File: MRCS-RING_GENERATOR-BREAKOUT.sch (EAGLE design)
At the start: 9 parts

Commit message: Various updates while preparing documentation
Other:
- note added: "F connections for PCR SIN01 FO F1 0 0 25 Hz 0 1 17 Hz 1 = JMP to 5VREF"
- note removed: "F connections for PCR SIN06 FO F1 0 0 20Hz 0 1 25 Hz 1 0 17 Hz 1 1 50 Hz 0 = OPEN 1 = JMP to 5VREF doesn't seem to work for SIN01, F0-F1 sit near ground and pulling up to 5 or 12 doesn't change freq or Vout"
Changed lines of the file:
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@@
 <text x="241.3" y="6.35" size="2.1844" layer="97">A</text>
 <text x="166.37" y="6.35" size="2.1844" layer="97">Seth Neumann</text>
-<text x="5.08" y="7.62" size="1.778" layer="97">F connections for PCR SIN06
+<text x="5.08" y="7.62" size="1.778" layer="97">F connections for PCR SIN01
 FO F1
-0  0  20Hz
-0  1  25 Hz
-1  0  17 Hz
-1  1   50 Hz
-0 = OPEN
-1 = JMP to 5VREF
-doesn't seem to work for SIN01, F0-F1 sit near ground
-and pulling up to 5 or 12 doesn't change freq or Vout</text>
+0  0  25 Hz
+0  1  17 Hz
+1 = JMP to 5VREF</text>
 <text x="129.54" y="157.48" size="1.778" layer="91">F1     F0</text>
 <text x="91.44" y="124.46" size="1.778" layer="91">pads for 0.1",

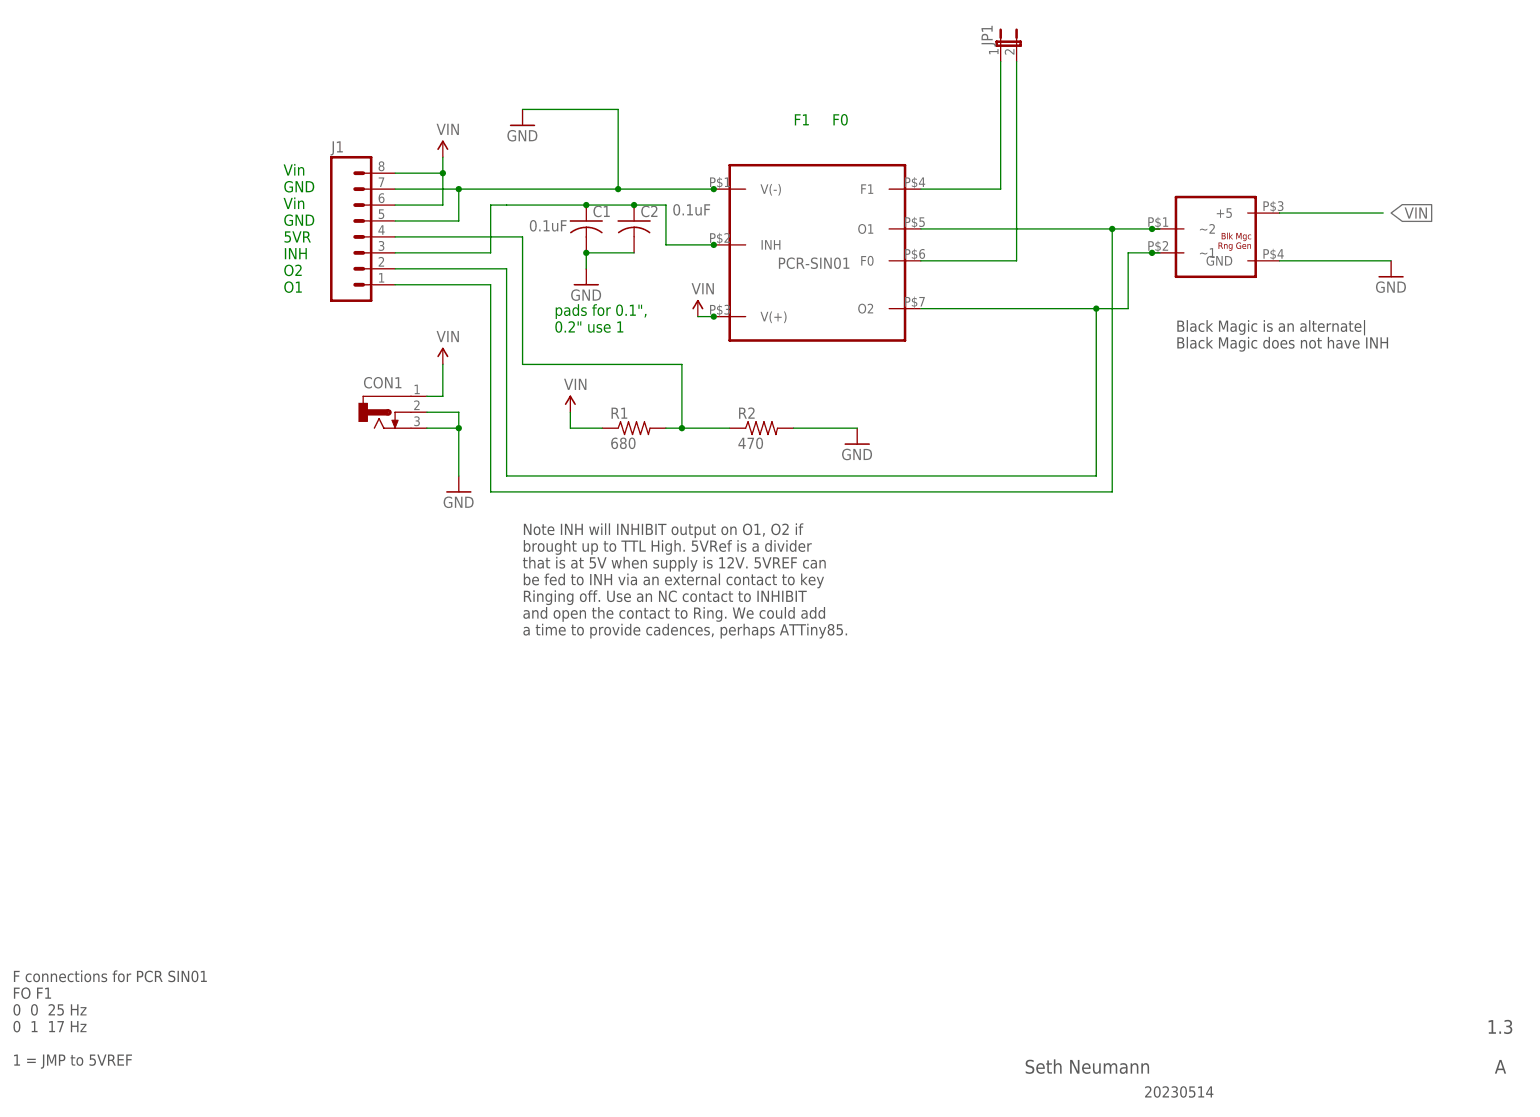
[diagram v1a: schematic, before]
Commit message: panelized 2 up version
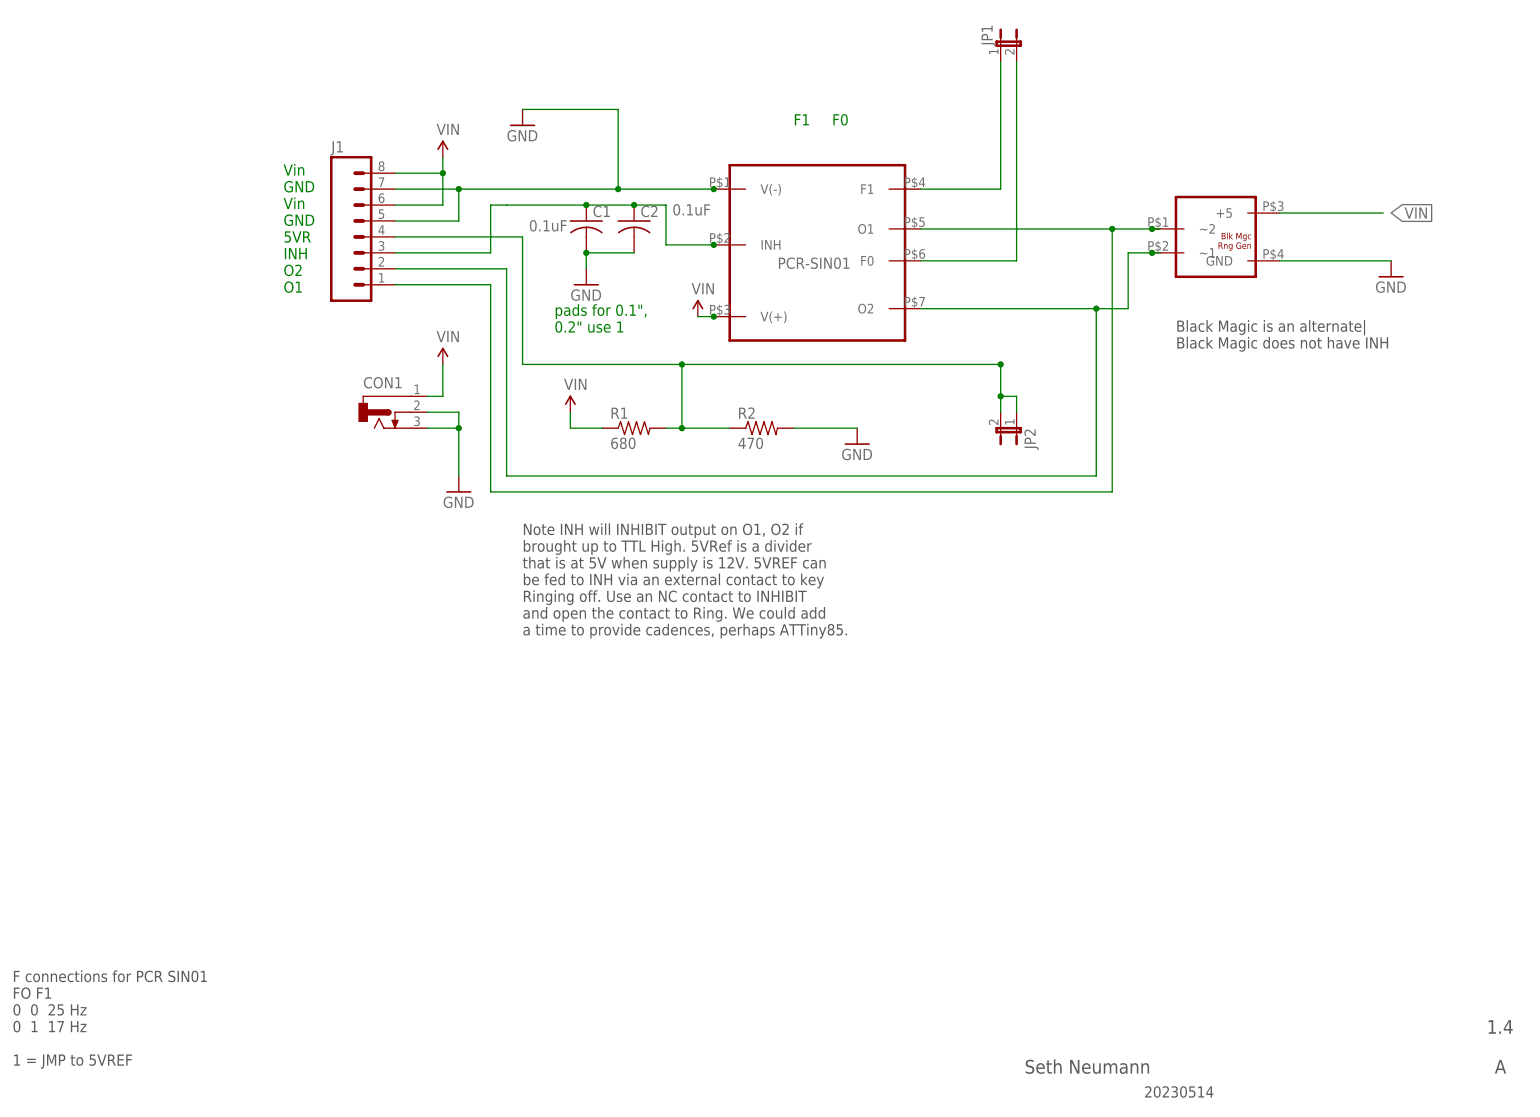
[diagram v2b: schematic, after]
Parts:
- added JP2: (no value), SPCoast:JUMPER-2PTH_LOCK
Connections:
- net 5VREF: now also JP2.1, JP2.2
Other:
- note added: "1.4"
- note removed: "1.3"
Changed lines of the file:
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@@
 <part name="U$5" library="MRCS" deviceset="BLACK_MAGIC_RING_GEN" device=""/>
 <part name="GND3" library="SPCoast" deviceset="GND" device=""/>
+<part name="JP2" library="SPCoast" deviceset="JUMPER-2" device="PTH_LOCK"/>
 </parts>
 <sheets>
 <sheet>
 <plain>
-<text x="240.03" y="12.7" size="2.1844" layer="97">1.3</text>
+<text x="240.03" y="12.7" size="2.1844" layer="97">1.4</text>
 <text x="241.3" y="6.35" size="2.1844" layer="97">A</text>
 <text x="166.37" y="6.35" size="2.1844" layer="97">Seth Neumann</text>
@@
 <instance part="U$5" gate="G$1" x="203.2" y="146.05" rot="R180"/>
 <instance part="GND3" gate="1" x="224.79" y="133.35"/>
+<instance part="JP2" gate="A" x="165.1" y="109.22" rot="R180"/>
 </instances>
 <busses>
@@
 <pinref part="J1" gate="G$1" pin="4"/>
 <wire x1="66.04" y1="139.7" x2="86.36" y2="139.7" width="0.3048" layer="91"/>
-</segment>
-</net>
+<wire x1="111.76" y1="119.38" x2="162.56" y2="119.38" width="0.3048" layer="91"/>
+<wire x1="162.56" y1="119.38" x2="162.56" y2="114.3" width="0.3048" layer="91"/>
+<wire x1="162.56" y1="114.3" x2="165.1" y2="114.3" width="0.3048" layer="91"/>
+<junction x="111.76" y="119.38"/>
+<junction x="162.56" y="119.38"/>
+<wire x1="165.1" y1="114.3" x2="165.1" y2="111.76" width="0.3048" layer="91"/>
+<wire x1="162.56" y1="114.3" x2="162.56" y2="111.76" width="0.3048" layer="91"/>
+<junction x="162.56" y="114.3"/>
+<pinref part="JP2" gate="A" pin="1"/>
+<pinref part="JP2" gate="A" pin="2"/>
+</segment>
+</net>
